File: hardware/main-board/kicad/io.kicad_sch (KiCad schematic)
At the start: 26 parts, among them J401 TF-015, J402 PANEL_UI, J403 OLED, J404 NTC, Q401 AO3401A, Q402 AO3400A, U401 BMI088

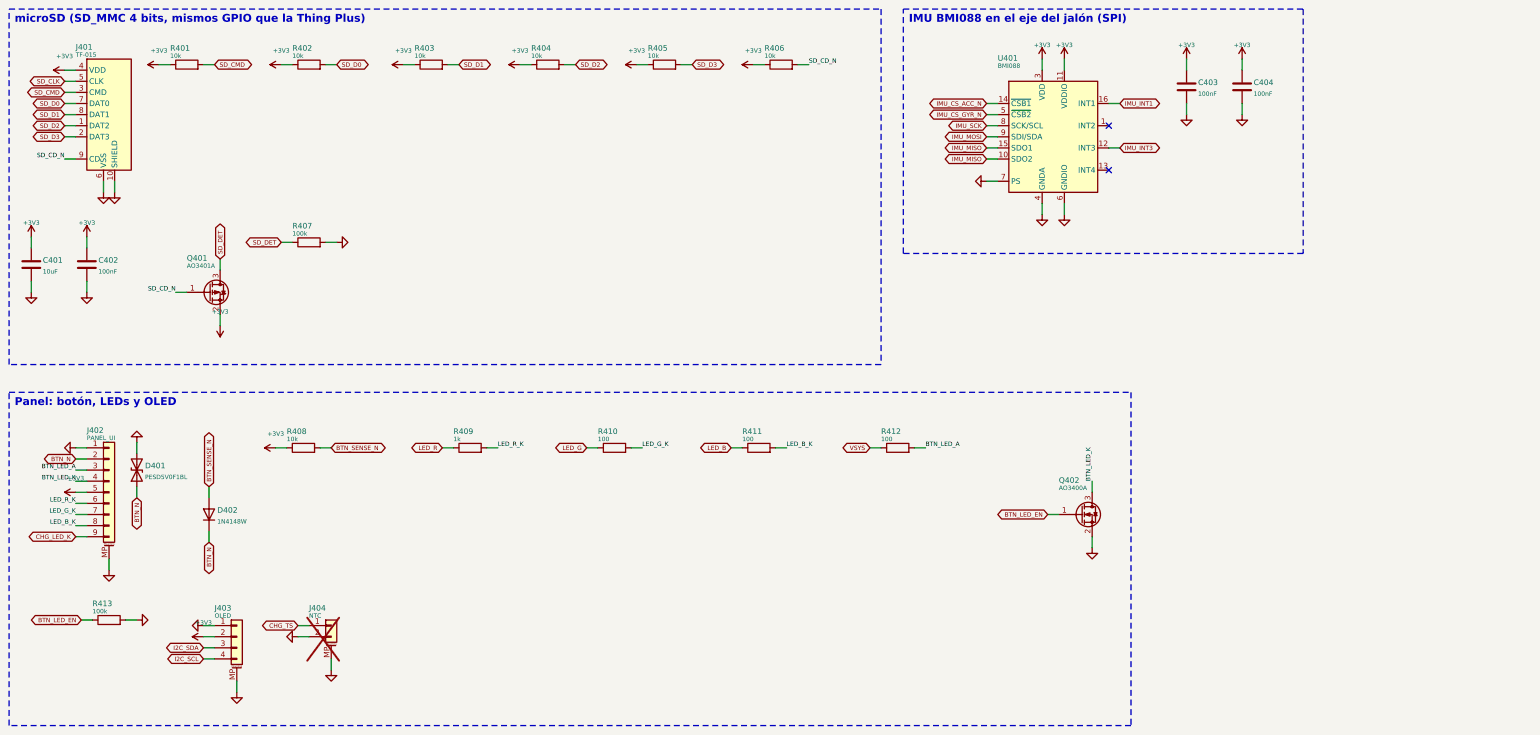
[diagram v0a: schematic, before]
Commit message: Placa principal v0.2: UM980 y BMI088 por cable, conectores hacia cantos o zonas libres, placa panel-usb y un solo panel para JLCPCB
- 46 x 64 mm, 4 capas. El UM980 queda en su carrier BDLX por J301 (GH 8) con 5 V conmutable
  (TPS63070, GPIO45) y el BMI088 vuelve a la tapa por I2C en un segundo bus (J405, GH 7).
- Todos los conectores de cable son GH o SH de 8 pines o menos (kit del propietario), salvo la
  batería (PH 2). Cada uno apunta a un canto o a una zona libre con sitio para la clavija
  enchufada y su cable: áreas de regla clavija_* en el DRC y kicad/plugs.json para el CAD.
- La placa sube 2.5 mm en el tubo (z 23.5-87.5) para que las clavijas del canto inferior tengan
  7.6 mm hasta la base; rieles propuestos en z 39-90 y agujeros nuevos. Comprobada en FreeCAD
  contra V2.2 con modelos 3D y clavijas: sin choques.
- Cargador según el ejemplo de TI: bootstrap junto a sus pines (0.9 y 1.6 mm), salida en abanico
  de la fila inferior y potencia solo por capas externas.
- Placa panel-usb (USB-C a ras de la tapa del panel, GH 8 a J101) y panel de las dos placas con un
  BOM y un CPL (panelize.py, 82.8 x 78 mm).
- Serigrafía sin solapes (silk_clean.py) y logotipo de TresVizo con www.tresvizo.com.
- ERC 0; DRC con 0 errores, 0 avisos, 0 sin conectar y 0 diferencias de paridad en las dos
  placas y el panel. Costo estimado de montaje y piezas: 211 USD por 5 juegos en un panel, sin
  el PCB desnudo.
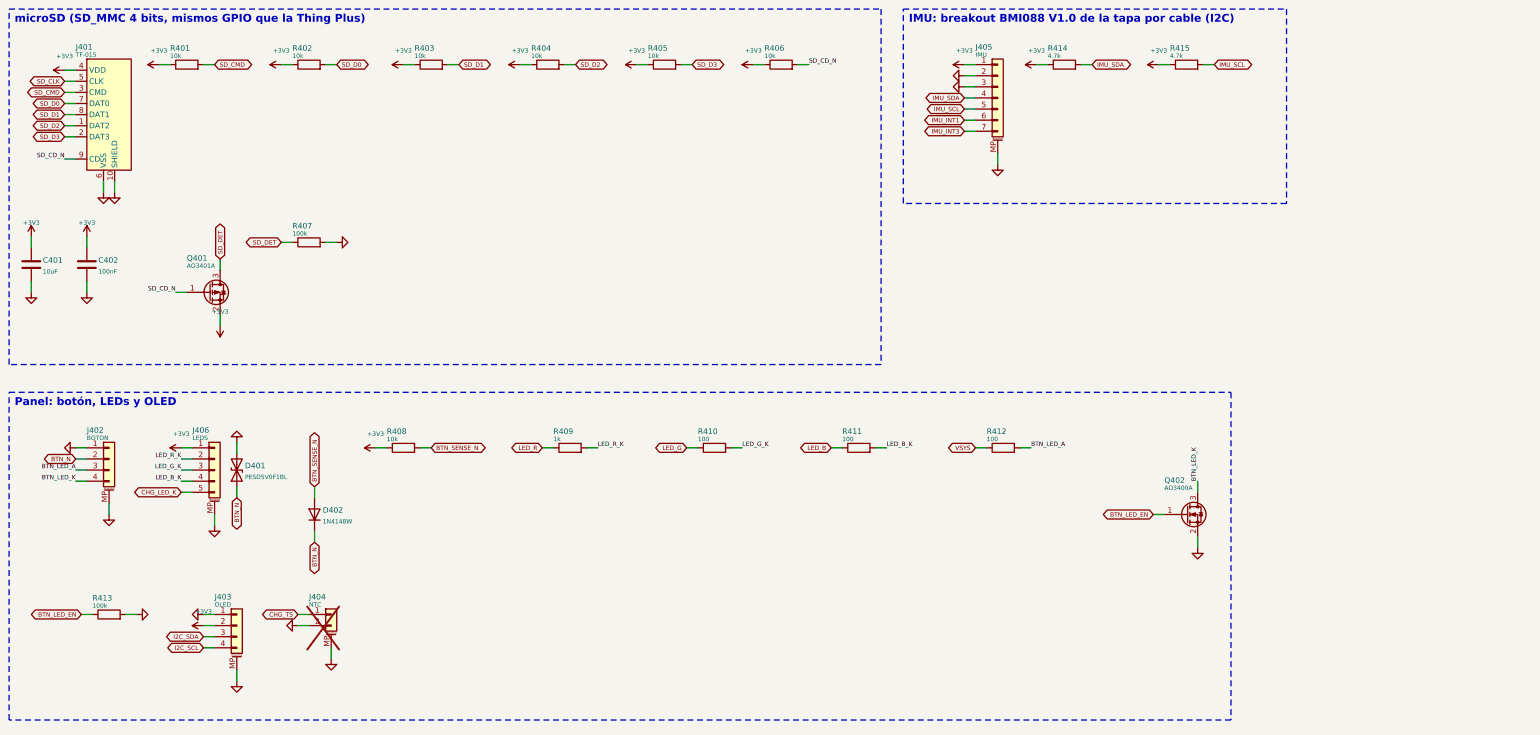
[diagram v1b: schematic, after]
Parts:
- removed C403, C404: 100nF, Capacitor_SMD:C_0402_1005Metric, symbol Device:C
- removed U401: BMI088, tresvizo_lcsc:LGA-16_L4.5-W3.0-P0.50-BL, symbol tresvizo:BMI088_SPI
- added J405: IMU, tresvizo_lcsc:CONN-SMD_SM7B-GHS-TB-LF-SN, symbol Connector_Generic_MountingPin:Conn_01x07_MountingPin
- added J406: LEDS, tresvizo_lcsc:CONN-SMD_SM05B-SRSS-TB-LF-SN, symbol Connector_Generic_MountingPin:Conn_01x05_MountingPin
- added R414, R415: 4.7k, Resistor_SMD:R_0402_1005Metric, symbol Device:R
- D401: LCSC C45961 -> C3001950; MPN PESD5V0F1BL,315 -> PESD5V0F1BL
- J402: value PANEL_UI -> BOTON; footprint tresvizo_lcsc:CONN-SMD_9P-P1.00_BM09B-SRSS-TB -> tresvizo_lcsc:CONN-SMD_4P-P1.25_SM04B-GHS-TB-LF-SN; symbol Connector_Generic_MountingPin:Conn_01x09_MountingPin -> Connector_Generic_MountingPin:Conn_01x04_MountingPin; LCSC C160395 -> C189895; MPN BM09B-SRSS-TB(LF)(SN) -> SM04B-GHS-TB(LF)(SN)
- J403: footprint tresvizo_lcsc:CONN-SMD_BM04B-SRSS-TB -> tresvizo_lcsc:CONN-SMD_4P-P1.00_SM04B-SRSS-TB-LF-SN; LCSC C160390 -> C160404; MPN BM04B-SRSS-TB(LF)(SN) -> SM04B-SRSS-TB(LF)(SN)
- J404: footprint tresvizo_lcsc:CONN-TH_BM02B-SRSS-TB-LF-SN -> tresvizo_lcsc:CONN-SMD_2P-P1.00_SM02B-SRSS-TB-LF-SN; LCSC C160388 -> C160402; MPN BM02B-SRSS-TB(LF)(SN) -> SM02B-SRSS-TB(LF)(SN)
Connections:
- net +3V3: now also J405.1 (Pin_1), J406.1 (Pin_1), R414.1, R415.1; no longer J402.5 (Pin_5)
- net CHG_LED_K: now also J406.5 (Pin_5); no longer J402.9 (Pin_9)
- net GND: now also J405.2 (Pin_2), J405.3 (Pin_3), J405.MP (MountPin), J406.MP (MountPin)
- net IMU_INT1: now also J405.6 (Pin_6)
- net IMU_INT3: now also J405.7 (Pin_7)
- net LED_B_K: now also J406.4 (Pin_4); no longer J402.8 (Pin_8)
- net LED_G_K: now also J406.3 (Pin_3); no longer J402.7 (Pin_7)
- net LED_R_K: now also J406.2 (Pin_2); no longer J402.6 (Pin_6)
- new net IMU_SCL: J405.5 (Pin_5), R415.2
- new net IMU_SDA: J405.4 (Pin_4), R414.2
- no-connect marks 2 -> 0
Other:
- note added: "IMU: breakout BMI088 V1.0 de la tapa por cable (I2C)"
- note removed: "IMU BMI088 en el eje del jalón (SPI)"
- title: microSD, IMU y panel -> microSD, IMU por conector y panel
- moved on the sheet: D401, D402, J403, J404, Q402, R408, R409, R410, R411, R412, R413

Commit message: Placa principal v0.2: J404 montado con puente JP101, USB-C de la panel-usb más volado, correcciones de la auditoría y logotipo
- J404 (NTC) se monta de fábrica y la NTC queda opcional. Sin ella, R106 (10 kΩ) va a GND por
  JP101, un puente de soldadura cerrado de fábrica, y el cargador ve 25 °C. Para usar la NTC se
  corta JP101 («cortar JP101» en la serigrafía, sobre el puente). R115 baja junto a R113 para
  dejar sitio a esa línea.
- panel-usb: el canto de la lengüeta retrocede 0.8 mm (v = 0.89) y el USB-C sobresale 1.29 mm; su
  cara sigue a ras de la tapa. El cobre queda a 0.41 mm del canto. En el panel la fresa frente al
  USB-C se ensancha a 3 mm (opción cuts de panelize.py) para dejar 1.71 mm hasta el marco; el
  panel pasa a 82.8 x 79 mm.
- Auditoría: VBUS de J101 al cargador con pistas de 0.8 y 1.0 mm, etiquetas de la batería y del
  NTC separadas, planos internos con 0.12 mm de margen y, en el README, medir el pin 1 de la
  carrier antes de enchufar el arnés y la ranura propuesta en la base bajo J102.
- Logotipo: las piezas con huecos se parten en tiras, porque KiCad deformaba al guardar los
  contornos fracturados (el distintivo de la cara de componentes salía mal).
- ERC 0; DRC con 0 errores, 0 avisos, 0 sin conectar y 0 diferencias de paridad en las dos placas
  y el panel. Comprobación en FreeCAD contra V2.2 sin choques nuevos. Costo estimado de montaje y
  piezas: 213.60 USD por 5 juegos en un panel (J404 suma 2.22 USD), sin el PCB desnudo.
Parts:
- J404: now fitted
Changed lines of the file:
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@@
 		(in_bom yes)
 		(on_board yes)
-		(dnp yes)
+		(dnp no)
 		(property "Reference" "J404"
 			(at 81.28 152.94 0)
@@
 			)
 		)
-		(property "Description" "Opcional: NTC 10k B3435 pegada a la celda (quitar el 10k fijo de TS)"
+		(property "Description" "NTC 10k B3435 opcional, pegada a la celda: al conectarla, cortar JP101"
 			(at 86.36 156.21 0)
 			(effects

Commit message: Placa principal v0.2: ESP32-S3-WROOM-1-N16R2 en lugar del MINI-1 y sin LEDs del panel
- U201 = ESP32-S3-WROOM-1-N16R2 (C2913205): 16 MB de flash y 2 MB de PSRAM quad. Huella y
  modelos de LCSC; el .step se corrió 3.65 mm para que coincida con su .wrl y la huella.
- GPIO nuevos para rutear el módulo en la misma placa: microSD CLK 6, CMD 7, D0 5, D1 4, D2 16,
  D3 15 y detección 17; UART del GNSS TX 8 / RX 9; PPS 10, EVENT 11, RESET 12; I2C 13/14;
  IMU 41/42 con INT1 2 e INT3 1; botón 18; puntos de prueba en 35, 36 y 37. README y pinout
  con el mapa para el firmware.
- Fuera J406, sus resistencias y la del STAT del cargador: la carcasa V2.3 no lleva LEDs.
- Misma placa de 46 x 64 mm. H1 pasa a (12.0, 9.6) y el corte del riel +X frente a la antena a
  v 15.1-34.0; antena sin cobre en u 0-6.7, v 15.7-33.7.
- R108 sale de debajo de los pines de la microSD (el ruteador se ciclaba entre SD_D3 y
  CHG_INT_N) y el divisor de TS va bajo L102.
- BUCK_SW y el PGND de U105 prerruteados: la vía que el ruteador ponía junto a L102 hacía caer
  el relleno de zonas de KiCad 10 (-11, también en kicad-cli). route_rest guarda las pistas que
  arranca mientras dura el ruteo.
- DRC 0, sin conexiones pendientes y con paridad en la placa y en el panel; ERC 0. Costo
  estimado 206.86 USD por 5 juegos (montaje + piezas, sin PCB).
- Carcasa V2.3: H1 en z 77.9, riel +X cortado en z 53.7-72.4, placa superior recortada frente
  a la antena y SMA de la carrier con las medidas de la foto. Placa nueva contra la carcasa:
  0 mm3 de choques.
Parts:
- removed J406: LEDS, tresvizo_lcsc:CONN-SMD_SM05B-SRSS-TB-LF-SN, symbol Connector_Generic_MountingPin:Conn_01x05_MountingPin
- removed R413: 100k, Resistor_SMD:R_0402_1005Metric, symbol Device:R
- removed R414, R415: 4.7k, Resistor_SMD:R_0402_1005Metric, symbol Device:R
- R409: value 1k -> 100; LCSC C11702 -> C25076; MPN 0402WGF1001TCE -> 0402WGF1000TCE
- R410: value 100 -> 100k; LCSC C25076 -> C25741; MPN 0402WGF1000TCE -> 0402WGF1003TCE
- R411, R412: value 100 -> 4.7k; LCSC C25076 -> C25900; MPN 0402WGF1000TCE -> 0402WGF4701TCE
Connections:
- net LED_B is gone; now on net +3V3: R411.1
- net LED_B_K is gone; now on net IMU_SDA: R411.2
- net LED_G is gone; now on net BTN_LED_EN: R410.1
- net LED_G_K is gone; now on net GND: R410.2
- net LED_R is gone; now on net VSYS: R409.1
- net LED_R_K is gone; now on net BTN_LED_A: R409.2
- net +3V3: now also R412.1
- net BTN_LED_A: no longer R412.2
- net IMU_SCL: now also R412.2
- net VSYS: no longer R412.1
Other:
- moved on the sheet: D401, D402, J403, J404, Q402, R408, R409, R410, R411, R412

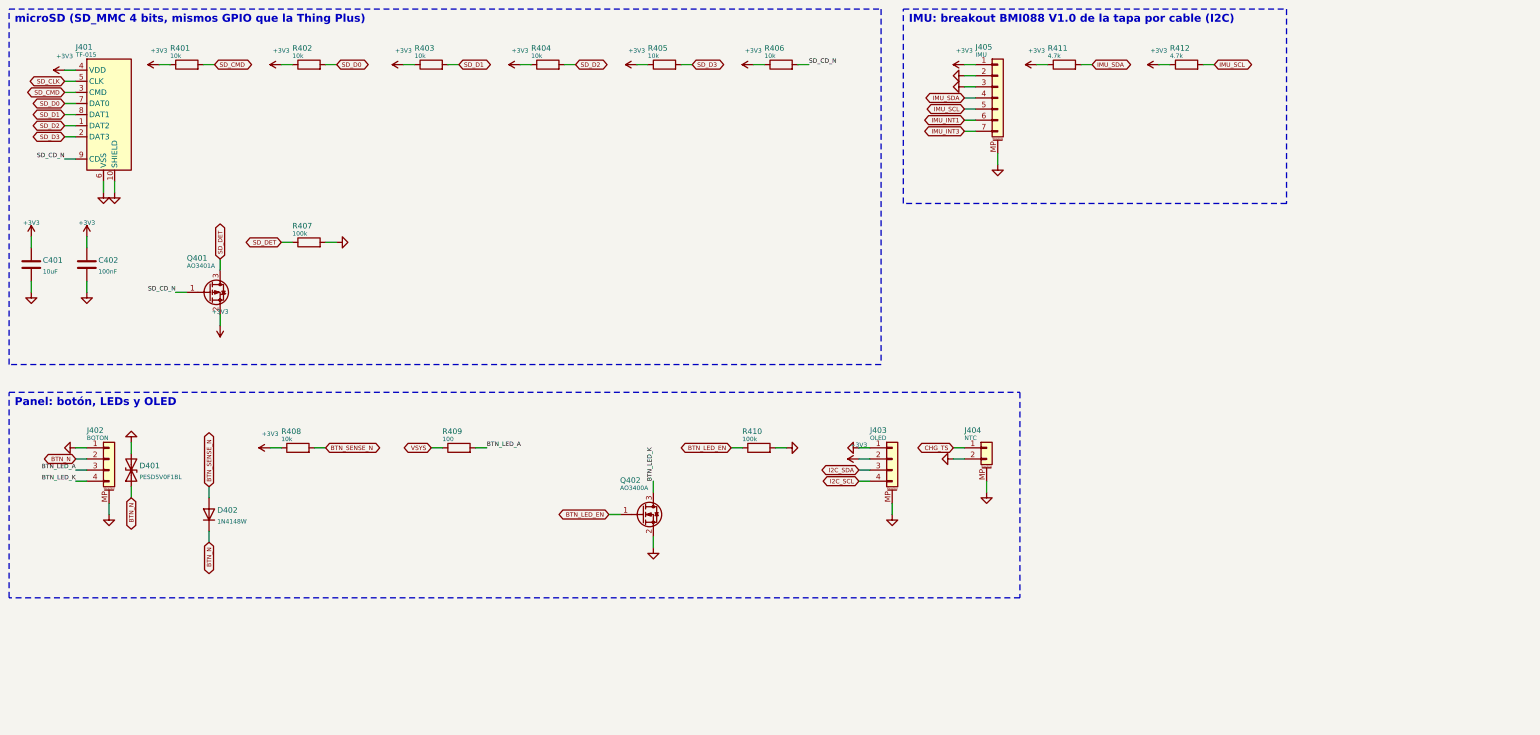
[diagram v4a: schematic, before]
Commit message: Placa principal v0.3 compacta: 36 × 71.5 mm para el tubo de Ø52, con USB-C, OLED, botón, LED y BMI088 en la placa
- Rama exploratoria pedida por el propietario el 07-10-2026. Especificación, interfaces con la
  carcasa, colocación y auditoría en research/v03-compacta.md.
- Esquema (ERC 0):
  - USB-C TYPE-C-31-M-12 con Rd de 5.1k, TVS SMF15A y USBLC6;
  - pulsador TS-1187A a BTN_N;
  - LED de estado en GPIO48 con 330 Ω;
  - OLED del propietario soldada sobre pads SMD (J403);
  - BMI088 por I2C (GPIO41/42, INT1 en GPIO2 e INT3 en GPIO1);
  - J102 en GH 4, con dos contactos por polo;
  - TP208 y TP209 en la UART0.
  Fuera J402, J405 y Q402; la panel-usb ya no se usa.
- Placa de 4 capas con muescas para la funda del USB-C y para la clavija SMA de la carrier.
  - Los bloques del cargador y de los reguladores se mueven sin cambiar su geometría interna.
  - La antena del WROOM va hacia −X, con zona sin cobre.
  - Panel de una sola placa.
  - DRC con 0 violaciones, 0 sin conectar y 0 de paridad; el panel, igual.
- Auditoría eléctrica independiente (08-10-2026), con sus siete puntos corregidos:
  - las soldaduras de la OLED ya no quedan frente al SMA de la carrier;
  - puentes del panel lejos del IMU y de los condensadores de potencia;
  - zona sin cobre de la antena más grande;
  - GND de J102 y vías dobles en VPACK;
  - vías junto al pad de tierra del WROOM;
  - LED más brillante;
  - pads de la UART.
- cad/export_board_step.py exporta el STEP en los ejes de la carcasa, con los modelos de LCSC
  corregidos. cad/check_heights.py comprueba los altos contra el tubo: todas las piezas caben con
  0.3 mm de aire.
- Cambios en los scripts:
  - route_rest.py admite límites de búsqueda por entorno;
  - fanout.py respeta las vías prerruteadas;
  - finish_pcb.py --final quita las vías sin uso;
  - cost_jlc.py sirve para una sola placa.
- Costo estimado en JLCPCB: 236.43 USD por 5 placas montadas, sin el PCB ni el envío.
- El build casi siempre se repite igual. En una de cuatro corrid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
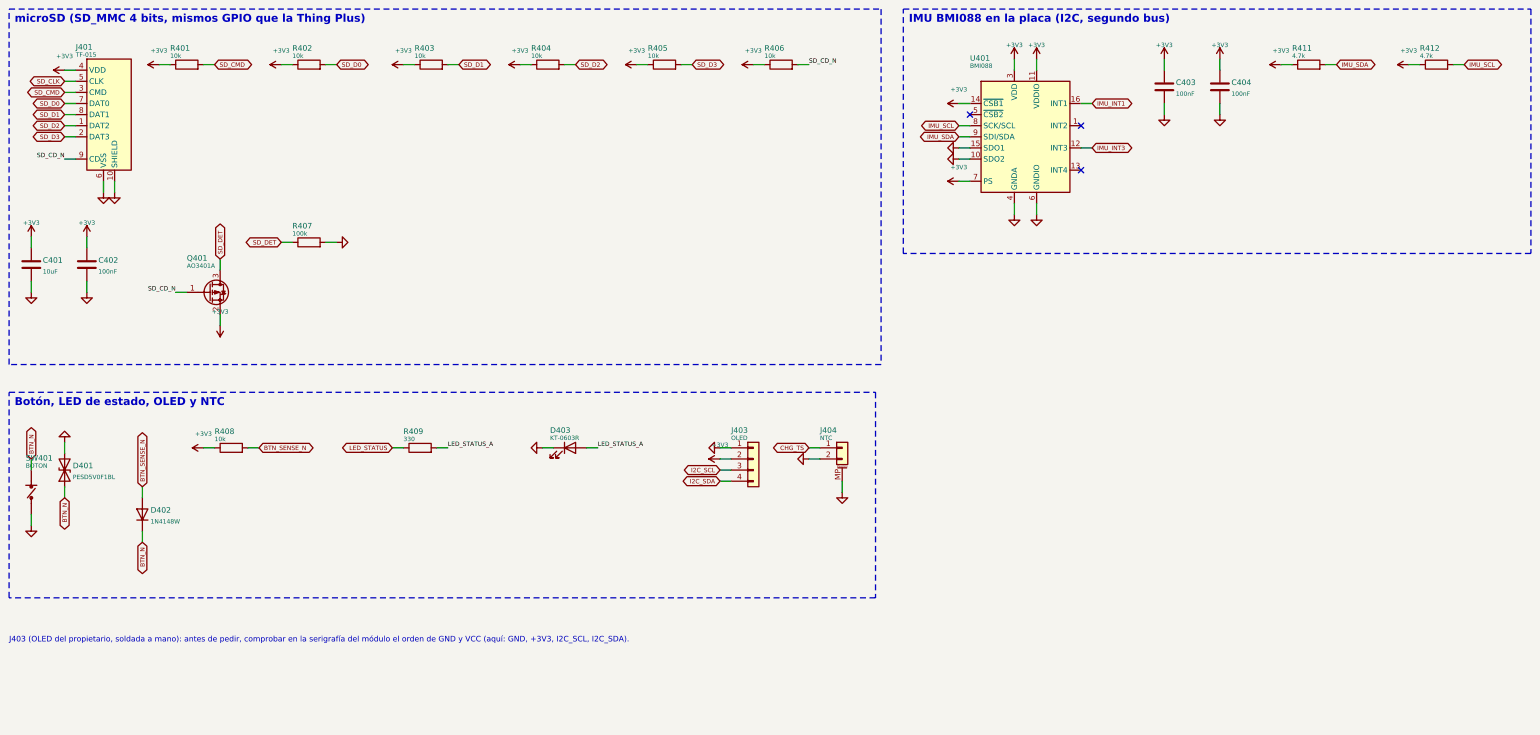
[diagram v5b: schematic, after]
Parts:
- removed J402: BOTON, tresvizo_lcsc:CONN-SMD_4P-P1.25_SM04B-GHS-TB-LF-SN, symbol Connector_Generic_MountingPin:Conn_01x04_MountingPin
- removed J405: IMU, tresvizo_lcsc:CONN-SMD_SM7B-GHS-TB-LF-SN, symbol Connector_Generic_MountingPin:Conn_01x07_MountingPin
- removed Q402: AO3400A, tresvizo_lcsc:SOT-23-3_L2.9-W1.3-P1.90-LS2.4-BR, symbol Transistor_FET:AO3400A
- removed R410: 100k, Resistor_SMD:R_0402_1005Metric, symbol Device:R
- added C403, C404: 100nF, Capacitor_SMD:C_0402_1005Metric, symbol Device:C
- added D403: KT-0603R, tresvizo_lcsc:LED-SMD_L1.6-W0.8-R-RD, symbol Device:LED
- added SW401: BOTON, tresvizo_lcsc:SW-SMD_4P-L5.1-W5.1-P3.70-LS6.5-TL_H1.5, symbol tresvizo:SW_TACT
- added U401: BMI088, tresvizo_lcsc:LGA-16_L4.5-W3.0-P0.50-BL, symbol tresvizo:BMI088_I2C
- J403: footprint tresvizo_lcsc:CONN-SMD_4P-P1.00_SM04B-SRSS-TB-LF-SN -> tresvizo_lcsc:OLED_0.96in_I2C_4P_P2.54mm; symbol Connector_Generic_MountingPin:Conn_01x04_MountingPin -> Connector_Generic:Conn_01x04; LCSC C160404 -> (none); MPN SM04B-SRSS-TB(LF)(SN) -> (none); now left out of the parts list
- R409: value 100 -> 330; LCSC C25076 -> C25104; MPN 0402WGF1000TCE -> 0402WGF3300TCE
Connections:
- net +3V3: now also C403.1, C404.1, U401.11 (VDDIO), U401.14 (~{CSB1}), U401.3 (VDD), U401.7 (PS)
- net BTN_N: now also SW401.1 (A)
- net GND: now also C403.2, C404.2, D403.1 (K), SW401.4 (B), U401.10 (SDO2), U401.15 (SDO1), U401.2 (GNDA), U401.4 (GNDA), U401.6 (GNDIO); no longer J403.MP (MountPin)
- net I2C_SCL: now also J403.3 (Pin_3); no longer J403.4 (Pin_4)
- net I2C_SDA: now also J403.4 (Pin_4); no longer J403.3 (Pin_3)
- net IMU_INT1: now also U401.16 (INT1)
- net IMU_INT3: now also U401.12 (INT3)
- net IMU_SCL: now also U401.8 (SCK/SCL)
- net IMU_SDA: now also U401.9 (SDI/SDA)
- net BTN_LED_A renamed LED_STATUS_A
- net LED_STATUS_A: now also D403.2 (A)
- net VSYS renamed LED_STATUS
- new net: SW401.2 (NC), SW401.3 (NC)
- no-connect marks 0 -> 3
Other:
- note added: "Botón, LED de estado, OLED y NTC"
- note added: "IMU BMI088 en la placa (I2C, segundo bus)"
- note added: "J403 (OLED del propietario, soldada a mano): antes de pedir, comprobar en la serigrafía del módulo el orden de GND y VCC (aquí: GND, +3V3, I2C_SCL, I2C_SDA)."
- note removed: "IMU: breakout BMI088 V1.0 de la tapa por cable (I2C)"
- note removed: "Panel: botón, LEDs y OLED"
- title: microSD, IMU por conector y panel -> microSD, IMU, OLED, botón y LED
- moved on the sheet: D401, D402, J404, R408, R409, R411, R412
